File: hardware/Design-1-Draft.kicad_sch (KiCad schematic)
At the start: 32 parts, among them J1 Barrel_Jack_Switch, M1 WATERPUMP-1, M2 WATERPUMP-2, Q1 IRLZ44N, Q2 IRLZ44N, SW1 Button, U3 ADS1115IDGS, U5 Tang_Nano_9K

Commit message: modified schem, wala pang pcb
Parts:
- removed R4: 4.7k, Resistor_THT:R_Axial_DIN0207_L6.3mm_D2.5mm_P10.16mm_Horizontal, symbol Device:R
- added A1: Arduino_Nano_ESP32, Module:Arduino_Nano, symbol MCU_Module:Arduino_Nano_ESP32
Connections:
- net GND: now also A1.29 (GND), A1.4 (GND)
- net at C3.2, C4.2, R5.1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: now also A1.30 (VIN)
- net at R5.2, U3.10 (SCL): now also A1.23 (SDA/A4); no longer U5.11 (33_IOB23A)
- net at U5.7 (27_IOB11A): no longer U3.2 (ALERT/RDY)
- net at R6.1, U3.9 (SDA): now also A1.24 (SCL/A5); no longer U5.12 (34_IOB23B)
- net at U5.9 (29_IOB13A): now also A1.6 (D3)
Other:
- moved on the sheet: BZ1, C5, M1, M2, Q1, Q2, R10, R11, R12, R7, R8, R9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

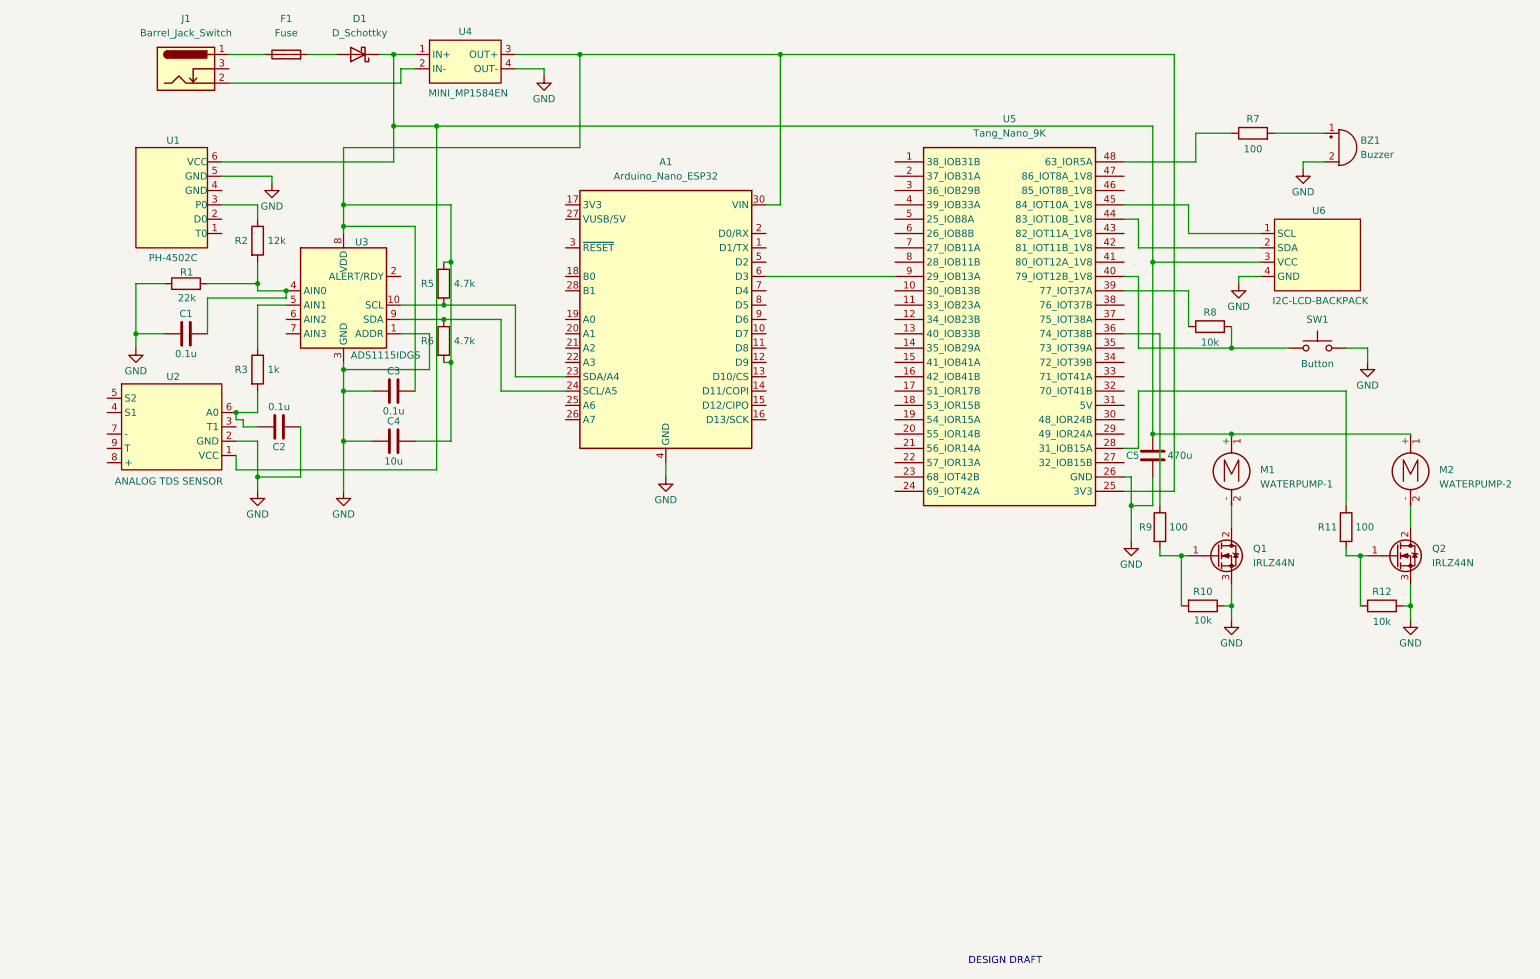
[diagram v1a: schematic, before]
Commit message: schem and symbols/footprint for shifter
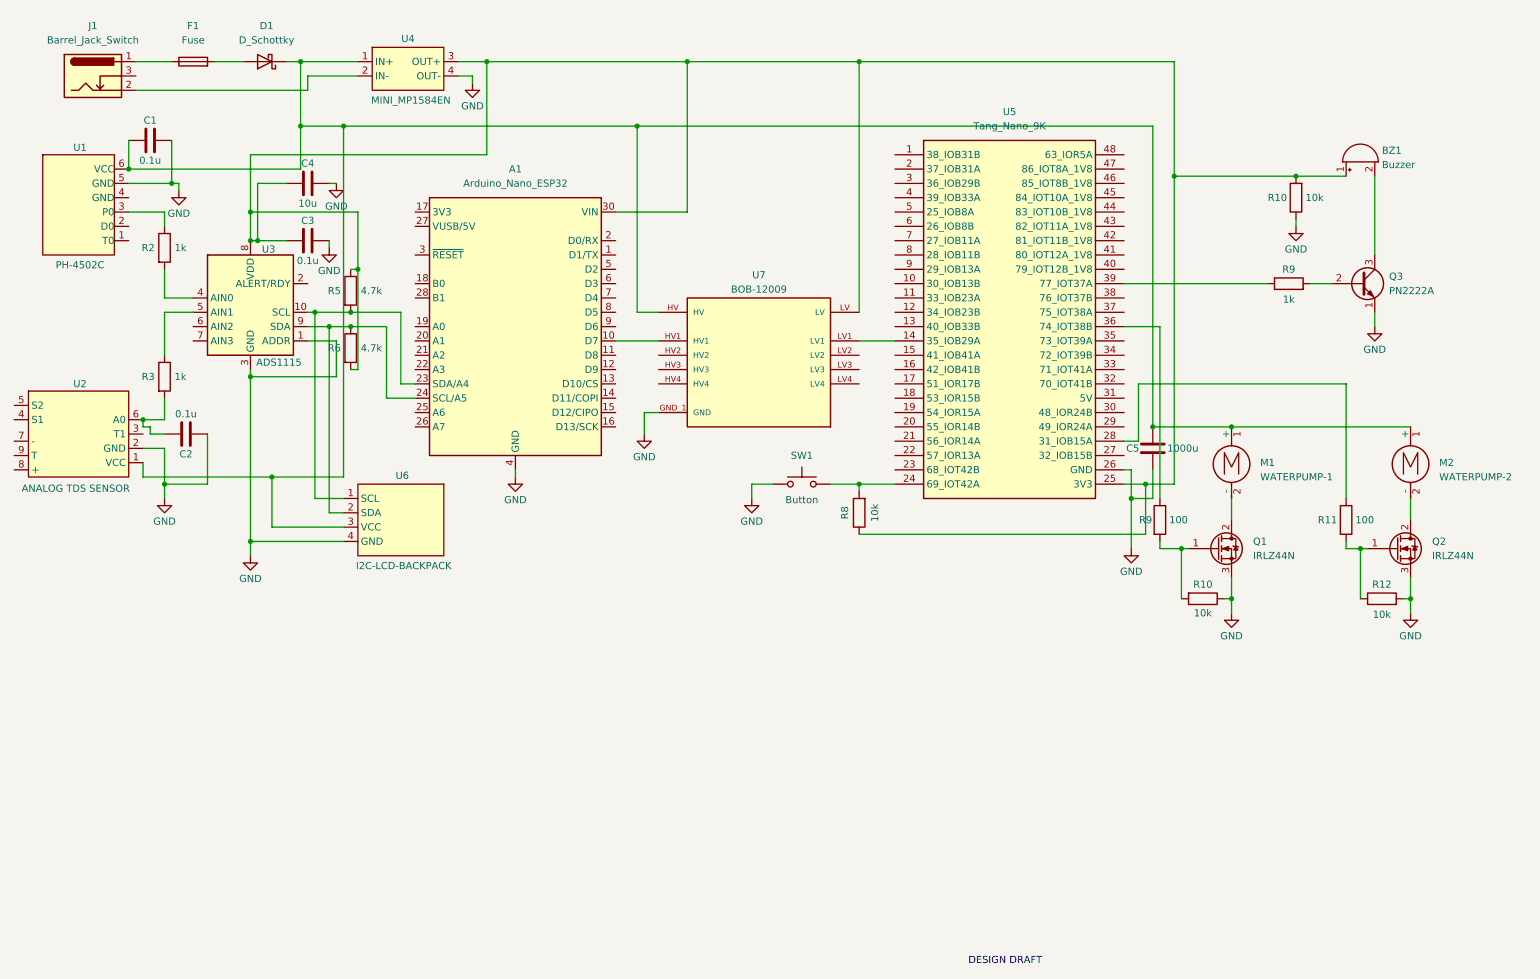
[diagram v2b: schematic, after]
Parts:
- removed R1: 22k, Resistor_THT:R_Axial_DIN0207_L6.3mm_D2.5mm_P10.16mm_Horizontal, symbol Device:R
- removed R7: 100, Resistor_THT:R_Axial_DIN0207_L6.3mm_D2.5mm_P10.16mm_Horizontal, symbol Device:R
- added Q3: PN2222A, Package_TO_SOT_THT:TO-92_Inline, symbol Transistor_BJT:PN2222A
- added R10: 10k, Resistor_THT:R_Axial_DIN0207_L6.3mm_D2.5mm_P10.16mm_Horizontal, symbol Device:R
- added R9: 1k, Resistor_THT:R_Axial_DIN0207_L6.3mm_D2.5mm_P10.16mm_Horizontal, symbol Device:R
- added U7: BOB-12009, BOB-12009:CONV_BOB-12009, symbol BOB-12009:BOB-12009
- C5: value 470u -> 1000u
- R2: value 12k -> 1k
- U3: value ADS1115IDGS -> ADS1115
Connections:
- net GND: now also C1.2, C3.2, C4.2, SW1.1, Q3.1 (E), R10.1, U7.GND_1 (GND), U7.GND_2 (GND); no longer BZ1.2 (-), C1.1, C3.1, C4.1, SW1.2
- net at C5.2, D1.1 (K), M1.1 (+)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: now also C1.1, U7.HV
- net at A1.30 (VIN), R5.1, R6.2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: now also BZ1.1 (+), C3.1, C4.1, R8.1, R10.2, U7.LV; no longer C3.2, C4.2
- net at R2.2, U3.4 (AIN0): no longer C1.2
- net at A1.23 (SDA/A4), R5.2, U3.10 (SCL): now also U6.1 (SCL)
- net at U5.14 (35_IOB29A): now also U7.LV1
- net at U5.24 (69_IOT42A): now also R8.2, SW1.2
- net at U5.39 (77_IOT37A): now also R9.1; no longer R8.1
- net at U5.44 (83_IOT10B_1V8): no longer U6.2 (SDA)
- net at U5.45 (84_IOT10A_1V8): no longer U6.1 (SCL)
- net at U5.9 (29_IOB13A): no longer A1.6 (D3)
- net at A1.24 (SCL/A5), R6.1, U3.9 (SDA): now also U6.2 (SDA)
- net at A1.10 (D7): now also U7.HV1
- new net: Q3.2 (B), R9.2
- new net: BZ1.2 (-), Q3.3 (C)
- now unconnected: U5.40 (79_IOT12B_1V8)
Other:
- moved on the sheet: A1, BZ1, C1, C2, C3, C4, C5, D1, F1, J1, M1, M2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

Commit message: revised schem, renamed GND symbols > GND zones, removed buck converter, 5V to arduino & adc
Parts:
- removed U4: ~, 1_CustomFootprints:SRT_MPT1584EN_Module, symbol 1_CustomSymbols:MINI_MP1584EN
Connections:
- net at C1.1, C5.2, D1.1 (K)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: now also A1.30 (VIN), BZ1.1 (+), C3.1, C4.1, R10.2, R5.1, R6.2, U3.8 (VDD), U5.31 (5V)
- net DGND: now reaches J1.2
- net DGND: now also A1.29 (GND), A1.4 (GND), SW1.1, U3.1 (ADDR), U3.3 (GND), U5.26 (GND), U6.4 (GND), U7.GND_1 (GND), U7.GND_2 (GND)
- removed net GND: A1.29 (GND), A1.4 (GND), C1.2, C2.1, C3.2, C4.2, C5.1, Q1.3 (S), Q2.3 (S), Q3.1 (E), R10.1, R10.1, R12.2, SW1.1, U1.5 (GND), U2.2 (GND), U3.1 (ADDR), U3.3 (GND), U5.26 (GND), U6.4 (GND), U7.GND_1 (GND), U7.GND_2 (GND)
- new net: R8.1, U5.25 (3V3), U7.LV
- new net AGND: C1.2, C2.1, C3.2, C4.2, U1.5 (GND), U2.2 (GND)
- new net PGND: C5.1, Q1.3 (S), Q2.3 (S), Q3.1 (E), R10.1, R10.1, R12.2
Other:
- moved on the sheet: R8, SW1
